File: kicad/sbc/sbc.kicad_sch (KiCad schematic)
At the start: 62 parts, among them CON1 BARREL_JACK, J1 USB, P1 USERPORT, SW1 SW_PUSH, U1 W65C02, U10 LM555N, U11 W65C22NxPL, U12 74HCT245, U13 74HCT245, U2 CHUCK, U3 AS6C4008, U4 28C256, U5 74LS06, X1 OSC

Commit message: DRC hell II
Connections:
- net GND: now also J1.5 (Shield)
- no-connect marks 44 -> 43
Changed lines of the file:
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@@
   (junction (at 113.03 266.7) (diameter 0) (color 0 0 0 0)
+  )
+  (junction (at 226.06 278.13) (diameter 0) (color 0 0 0 0)
   )
   (junction (at 151.13 266.7) (diameter 0) (color 0 0 0 0)
@@
   (no_connect (at 236.22 267.97))
   (no_connect (at 232.41 130.81))
-  (no_connect (at 226.06 275.59))
   (no_connect (at 232.41 128.27))
   (no_connect (at 318.77 242.57))
@@
     (stroke (width 0) (type default))
   )
-  (wire (pts (xy 201.93 278.13) (xy 228.6 278.13))
+  (wire (pts (xy 201.93 278.13) (xy 226.06 278.13))
     (stroke (width 0) (type default))
   )
@@
     (stroke (width 0) (type default))
   )
+  (wire (pts (xy 226.06 275.59) (xy 226.06 278.13))
+    (stroke (width 0) (type default))
+  )
   (wire (pts (xy 102.87 63.5) (xy 111.76 63.5))
     (stroke (width 0) (type default))
@@
     (stroke (width 0) (type default))
   )
+  (wire (pts (xy 226.06 278.13) (xy 228.6 278.13))
+    (stroke (width 0) (type default))
+  )

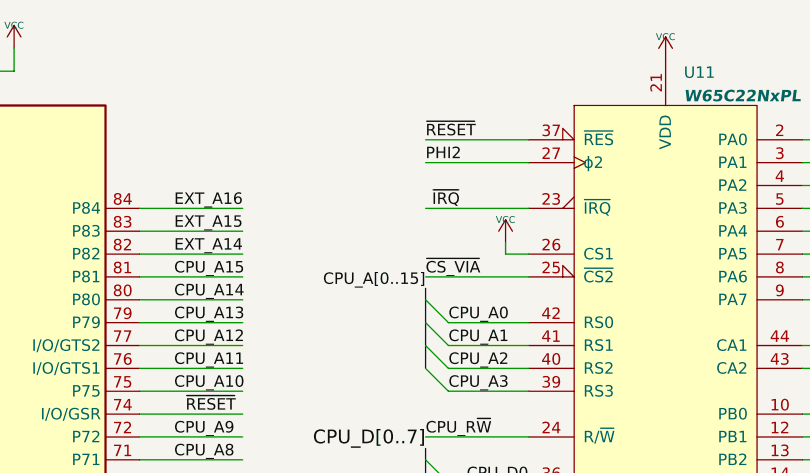
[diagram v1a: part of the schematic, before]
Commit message: added magic irq diode for W65c22S
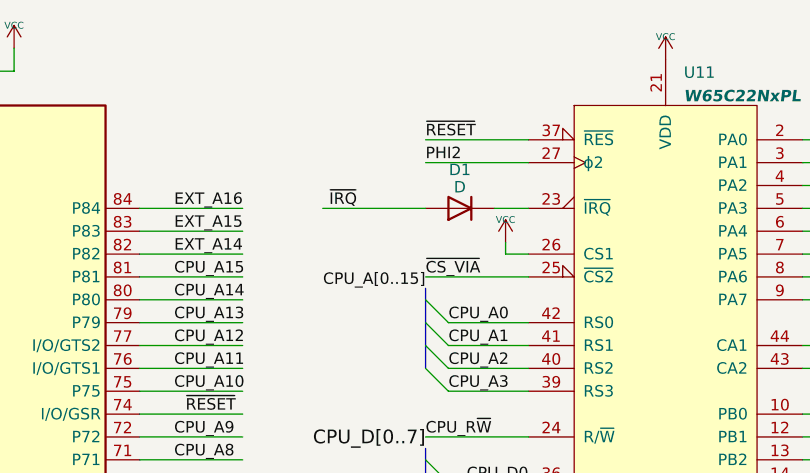
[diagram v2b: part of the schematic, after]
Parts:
- added D1: D, Diode_THT:D_DO-35_SOD27_P7.62mm_Horizontal, symbol Device:D
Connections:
- net ~{IRQ}: now also D1.2 (A); no longer U11.23 (~{IRQ})
- new net: D1.1 (K), U11.23 (~{IRQ})
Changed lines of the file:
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@@
     (stroke (width 0) (type default))
   )
-  (wire (pts (xy 252.73 39.37) (xy 264.16 39.37))
+  (wire (pts (xy 241.3 39.37) (xy 252.73 39.37))
     (stroke (width 0) (type default))
   )
@@
   )
   (bus (pts (xy 363.22 123.19) (xy 363.22 125.73))
+    (stroke (width 0) (type default))
+  )
+  (wire (pts (xy 260.35 39.37) (xy 264.16 39.37))
     (stroke (width 0) (type default))
   )
@@
     (effects (font (size 1.27 1.27)) (justify left bottom))
   )
-  (label "~{IRQ}" (at 256.54 39.37 180) (fields_autoplaced)
+  (label "~{IRQ}" (at 245.11 39.37 180) (fields_autoplaced)
     (effects (font (size 1.27 1.27)) (justify right bottom))
   )
@@
         )
       )
+    )
+  )
+  (symbol (lib_id "Device:D") (at 256.54 39.37 180) (unit 1)
+    (in_bom yes) (on_board yes) (dnp no) (fields_autoplaced)
+    (property "Reference" "D1" (at 256.54 35.0901 0)
+      (effects (font (size 1.27 1.27)))
+    )
+    (property "Value" "D" (at 256.54 37.0111 0)
+      (effects (font (size 1.27 1.27)))
+    )
+    (property "Footprint" "Diode_THT:D_DO-35_SOD27_P7.62mm_Horizontal" (at 256.54 39.37 0)
+      (effects (font (size 1.27 1.27)) hide)
+    )
+    (property "Datasheet" "~" (at 256.54 39.37 0)
+      (effects (font (size 1.27 1.27)) hide)
+    )
+    (property "Sim.Device" "D" (at 256.54 39.37 0)
+      (effects (font (size 1.27 1.27)) hide)
+    )
+    (property "Sim.Pins" "1=K 2=A" (at 256.54 39.37 0)
+      (effects (font (size 1.27 1.27)) hide)
+    )
+    (pin "1")
+    (pin "2")
+    (instances
+      (project "sbc"
+        (path "/896d5dab-44ec-47d0-8232-7ef57773545e"
+          (reference "D1") (unit 1)
+        )
+      )

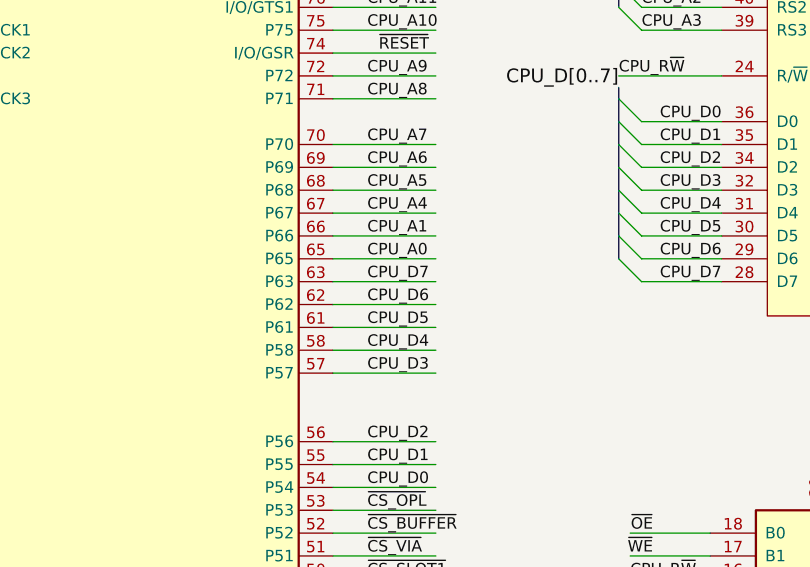
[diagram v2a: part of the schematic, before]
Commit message: regular sd socket separate masses for analog and digital cleanup routing
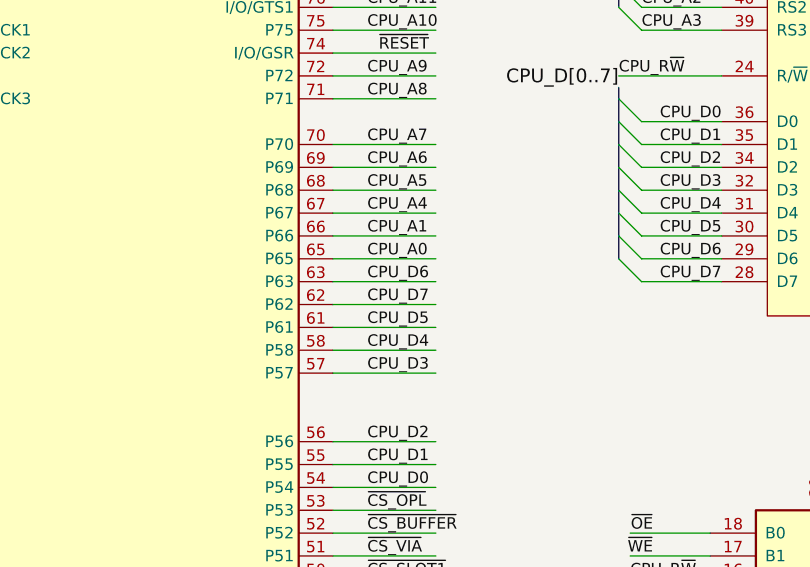
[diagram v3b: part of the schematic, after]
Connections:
- net CPU_D6: now also U2.63 (P63); no longer U2.62 (P62)
- net CPU_D7: now also U2.62 (P62); no longer U2.63 (P63)
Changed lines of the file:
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@@
     (effects (font (size 1.27 1.27)) (justify right bottom))
   )
-  (label "CPU_D6" (at 224.79 90.17 0) (fields_autoplaced)
+  (label "CPU_D6" (at 224.79 87.63 0) (fields_autoplaced)
     (effects (font (size 1.27 1.27)) (justify left bottom))
   )
@@
     (effects (font (size 1.27 1.27)) (justify right bottom))
   )
-  (label "CPU_D7" (at 224.79 87.63 0) (fields_autoplaced)
+  (label "CPU_D7" (at 224.79 90.17 0) (fields_autoplaced)
     (effects (font (size 1.27 1.27)) (justify left bottom))
   )

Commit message: cleanup
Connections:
- net GND: no longer SW1.4
- net RESET_TRIG: no longer SW1.3
- no-connect marks 43 -> 45
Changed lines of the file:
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@@
   (junction (at 201.93 270.51) (diameter 0) (color 0 0 0 0)
   )
-  (junction (at 82.55 260.35) (diameter 0) (color 0 0 0 0)
-  )
   (junction (at 125.73 266.7) (diameter 0) (color 0 0 0 0)
   )
@@
   (junction (at 109.22 215.9) (diameter 0) (color 0 0 0 0)
   )
-  (junction (at 82.55 270.51) (diameter 0) (color 0 0 0 0)
-  )
   (junction (at 119.38 266.7) (diameter 0) (color 0 0 0 0)
   )
@@
   (no_connect (at 166.37 67.31))
   (no_connect (at 236.22 267.97))
+  (no_connect (at 82.55 270.51))
   (no_connect (at 232.41 130.81))
   (no_connect (at 232.41 128.27))
@@
   (no_connect (at 30.48 80.01))
   (no_connect (at 166.37 90.17))
+  (no_connect (at 82.55 260.35))
   (no_connect (at 166.37 130.81))
   (no_connect (at 166.37 120.65))
@@
     (stroke (width 0) (type default))
   )
-  (wire (pts (xy 87.63 260.35) (xy 82.55 260.35))
-    (stroke (width 0) (type default))
-  )
   (wire (pts (xy 111.76 53.34) (xy 102.87 53.34))
     (stroke (width 0) (type default))
@@
     (stroke (width 0) (type default))
   )
-  (wire (pts (xy 82.55 251.46) (xy 82.55 260.35))
+  (wire (pts (xy 87.63 251.46) (xy 87.63 260.35))
     (stroke (width 0) (type default))
   )
@@
     (stroke (width 0) (type default))
   )
-  (wire (pts (xy 87.63 270.51) (xy 82.55 270.51))
-    (stroke (width 0) (type default))
-  )
   (bus (pts (xy 72.39 46.99) (xy 72.39 49.53))
     (stroke (width 0) (type default))
@@
     (stroke (width 0) (type default))
   )
-  (wire (pts (xy 82.55 270.51) (xy 82.55 278.13))
+  (wire (pts (xy 87.63 270.51) (xy 87.63 278.13))
     (stroke (width 0) (type default))
   )
@@
     (effects (font (size 1.27 1.27)) (justify left bottom))
   )
-  (label "RESET_TRIG" (at 82.55 254 0) (fields_autoplaced)
+  (label "RESET_TRIG" (at 87.63 254 0) (fields_autoplaced)
     (effects (font (size 1.27 1.27)) (justify left bottom))
   )
@@
     )
   )
-  (symbol (lib_id "power:GND") (at 82.55 278.13 0) (unit 1)
+  (symbol (lib_id "power:GND") (at 87.63 278.13 0) (unit 1)
     (in_bom yes) (on_board yes) (dnp no)
-    (property "Reference" "#PWR0111" (at 82.55 278.13 0)
+    (property "Reference" "#PWR0111" (at 87.63 278.13 0)
       (effects (font (size 0.762 0.762)) hide)
     )
-    (property "Value" "GND" (at 82.55 279.908 0)
+    (property "Value" "GND" (at 87.63 279.908 0)
       (effects (font (size 0.762 0.762)) hide)
     )
-    (property "Footprint" "" (at 82.55 278.13 0)
+    (property "Footprint" "" (at 87.63 278.13 0)
       (effects (font (size 1.27 1.27)) hide)
     )
-    (property "Datasheet" "" (at 82.55 278.13 0)
+    (property "Datasheet" "" (at 87.63 278.13 0)
       (effects (font (size 1.27 1.27)) hide)
     )

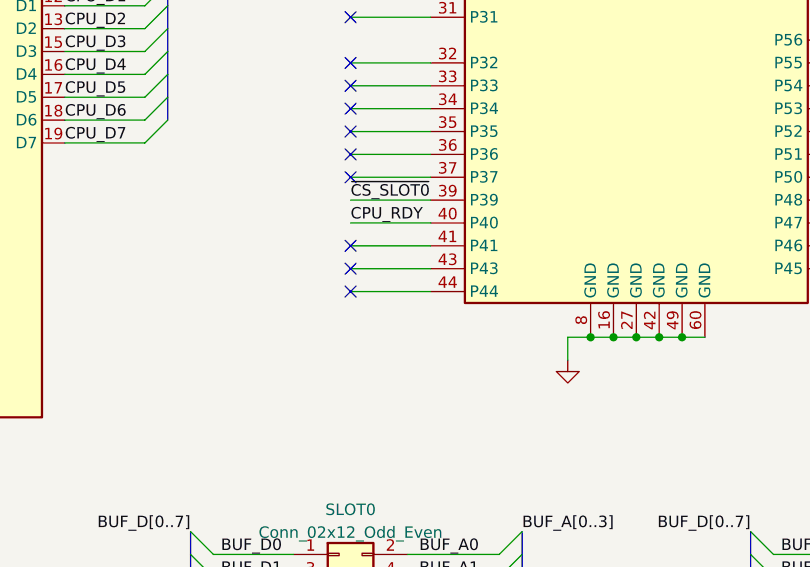
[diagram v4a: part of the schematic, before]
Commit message: connect cpu_r/W to CPLD
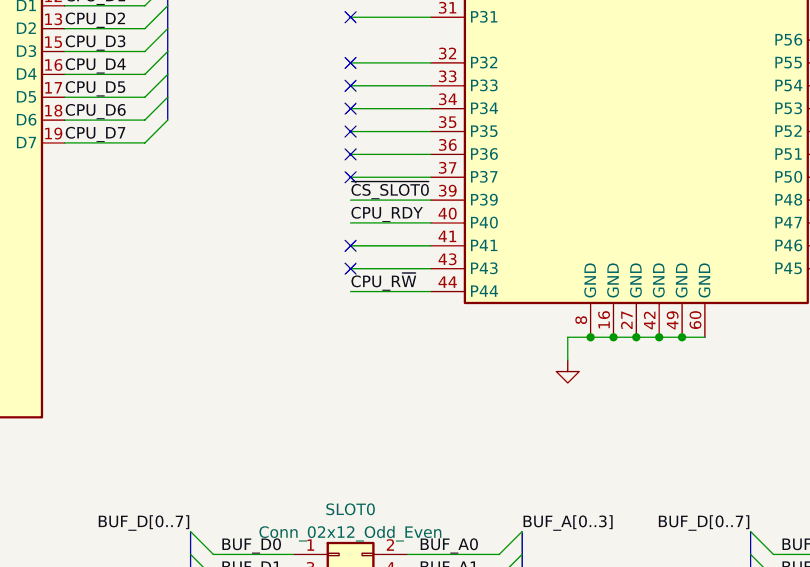
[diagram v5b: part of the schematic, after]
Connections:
- net CPU_R~{W}: now also U2.44 (P44)
- no-connect marks 45 -> 44
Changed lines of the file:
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@@
   (junction (at 90.17 215.9) (diameter 0) (color 0 0 0 0)
   )
-  (no_connect (at 166.37 133.35))
   (no_connect (at 166.37 107.95))
   (no_connect (at 30.48 44.45))
@@
     (effects (font (size 1.27 1.27)) (justify right bottom))
   )
+  (label "CPU_R~{W}" (at 166.37 133.35 0) (fields_autoplaced)
+    (effects (font (size 1.27 1.27)) (justify left bottom))
+  )
   (label "BUF_A3" (at 289.56 133.35 0) (fields_autoplaced)

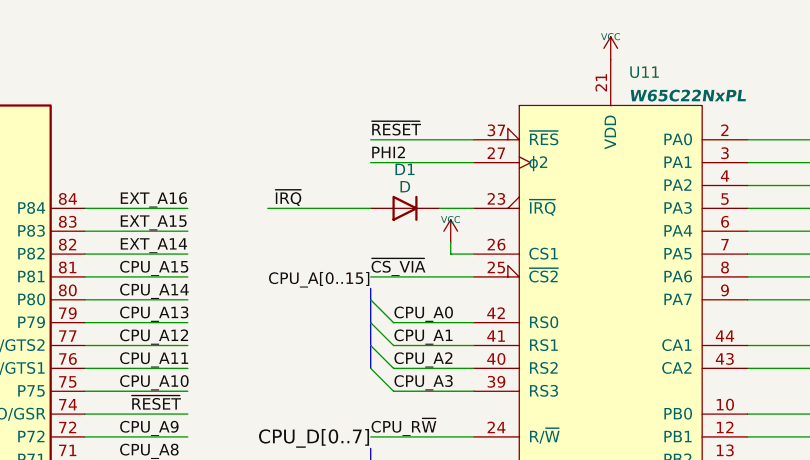
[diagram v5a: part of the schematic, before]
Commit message: moved all symbols into custom library
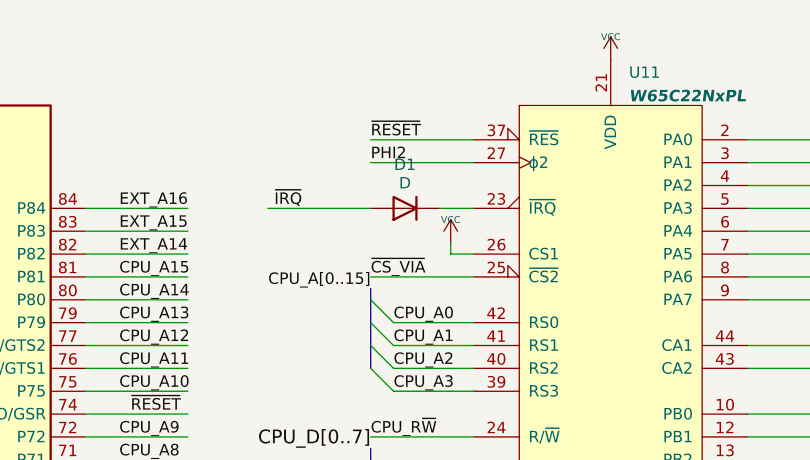
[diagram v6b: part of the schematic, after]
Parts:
- C1, C2: footprint Capacitor_THT:C_Disc_D3.0mm_W2.0mm_P2.50mm -> Capacitor_SMD:C_1206_3216Metric_Pad1.33x1.80mm_HandSolder; symbol Device:C -> steckschwein:C
- C10, C11, C12, C13, C14, C15, C16, C5, C57, C58, C59, C6, C60, C61, C62, C63, C7, C8, C9: symbol Device:C -> steckschwein:C
- C17, C4: footprint Capacitor_THT:CP_Radial_D4.0mm_P2.00mm -> Capacitor_THT:CP_Radial_D10.0mm_P5.00mm; symbol Device:C_Polarized -> steckschwein:C_Polarized
- C18, C3: symbol Device:C_Polarized -> steckschwein:C_Polarized
- CON1: symbol Connector:Barrel_Jack -> steckschwein:Barrel_Jack
- D1: symbol Device:D -> steckschwein:D
- J1: symbol Connector:USB_B -> steckschwein:USB_B
- JP1: symbol Jumper:Jumper_3_Bridged12 -> steckschwein:Jumper_3_Bridged12
- JTAG1: symbol Connector:Conn_01x06_Pin -> steckschwein:Conn_01x06_Pin
- P1: symbol Connector_Generic:Conn_02x08_Odd_Even -> steckschwein:Conn_02x08_Odd_Even
- R1, R10, R11, R12, R13, R15, R2, R3, R4, R5, R6, R7, R8, R9: symbol Device:R -> steckschwein:R
- RN1: symbol Device:R_Network04 -> steckschwein:R_Network04
- SLOT0, SLOT1: symbol Connector_Generic:Conn_02x12_Odd_Even -> steckschwein:Conn_02x12_Odd_Even
- SW1: symbol Switch:SW_Push_Dual -> steckschwein:SW_Push_Dual
- U1: symbol 65xx:W65C02SxPL -> steckschwein:W65C02SxPL
- U11: symbol 65xx:W65C22NxPL -> steckschwein:W65C22NxPL
- U12, U13: symbol 74xx:74HC245 -> steckschwein:74HC245
- U2: symbol CPLD_Xilinx:XC95108PC84 -> steckschwein:XC95108PC84
- U3: symbol Memory_RAM:AS6C4008-55PCN -> steckschwein:AS6C4008-55PCN
- U4: symbol Memory_EEPROM:28C256 -> steckschwein:28C256
- U5: symbol 74xx:74LS06 -> steckschwein:74LS06
- X1: symbol osc:OSC -> steckschwein:OSC

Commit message: moved all footprints into local library
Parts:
- C1, C2: footprint Capacitor_SMD:C_1206_3216Metric_Pad1.33x1.80mm_HandSolder -> steckschwein:C_Disc_D3.0mm_W2.0mm_P2.50mm
- C10, C11, C12, C13, C14, C15, C16, C5, C57, C58, C59, C6, C60, C61, C62, C63, C7, C8, C9: footprint Capacitor_SMD:C_1206_3216Metric_Pad1.33x1.80mm_HandSolder -> steckschwein:C_1206_3216Metric_Pad1.33x1.80mm_HandSolder
- C17, C4: footprint Capacitor_THT:CP_Radial_D10.0mm_P5.00mm -> steckschwein:CP_Radial_D4.0mm_P2.00mm
- C18, C3: footprint Capacitor_THT:CP_Radial_D10.0mm_P5.00mm -> steckschwein:CP_Radial_D10.0mm_P5.00mm
- CON1: footprint Connector_BarrelJack:BarrelJack_Horizontal -> steckschwein:BarrelJack_Horizontal
- D1: footprint Diode_THT:D_DO-35_SOD27_P7.62mm_Horizontal -> steckschwein:D_DO-35_SOD27_P7.62mm_Horizontal
- H1, H2, H3, H4: footprint MountingHole:MountingHole_3.2mm_M3 -> steckschwein:MountingHole_3.2mm_M3
- J1: footprint Connector_USB:USB_B_OST_USB-B1HSxx_Horizontal -> steckschwein:USB_B_OST_USB-B1HSxx_Horizontal
- JP1: footprint Connector_PinHeader_2.54mm:PinHeader_1x03_P2.54mm_Vertical -> steckschwein:PinHeader_1x03_P2.54mm_Vertical
- JTAG1: footprint Connector_PinHeader_2.54mm:PinHeader_1x06_P2.54mm_Vertical -> steckschwein:PinHeader_1x06_P2.54mm_Vertical
- P1: footprint Connector_PinHeader_2.54mm:PinHeader_2x08_P2.54mm_Horizontal -> steckschwein:PinHeader_2x08_P2.54mm_Horizontal
- R1, R10, R11, R12, R13, R15, R2, R3, R4, R5, R6, R7, R8, R9: footprint Resistor_THT:R_Axial_DIN0204_L3.6mm_D1.6mm_P5.08mm_Horizontal -> steckschwein:R_Axial_DIN0204_L3.6mm_D1.6mm_P7.62mm_Horizontal
- RN1: footprint Resistor_THT:R_Array_SIP5 -> steckschwein:R_Array_SIP5
- SLOT0, SLOT1: footprint Connector_PinSocket_2.54mm:PinSocket_2x12_P2.54mm_Vertical -> steckschwein:PinSocket_2x12_P2.54mm_Vertical
- SW1: footprint Button_Switch_THT:SW_SPST_Omron_B3F-315x_Angled -> steckschwein:SW_SPST_Omron_B3F-315x_Angled
- U1, U11: footprint Package_LCC:PLCC-44_THT-Socket -> steckschwein:PLCC-44_THT-Socket
- U10: footprint Package_DIP:DIP-8_W7.62mm_LongPads -> steckschwein:DIP-8_W7.62mm_LongPads
- U12, U13: footprint Package_DIP:DIP-20_W7.62mm_LongPads -> steckschwein:DIP-20_W7.62mm_LongPads
- U2: footprint Package_LCC:PLCC-84_THT-Socket -> steckschwein:PLCC-84_THT-Socket
- U3: footprint Package_DIP:DIP-32_W15.24mm_Socket_LongPads -> steckschwein:DIP-32_W15.24mm_Socket_LongPads
- U4: footprint Package_DIP:DIP-28_W15.24mm_Socket_LongPads -> steckschwein:DIP-28_W15.24mm_Socket_LongPads
- U5: footprint Package_DIP:DIP-14_W7.62mm_LongPads -> steckschwein:DIP-14_W7.62mm_LongPads
- X1: footprint Oscillator:Oscillator_DIP-14_LargePads -> steckschwein:Oscillator_DIP-14_LargePads
